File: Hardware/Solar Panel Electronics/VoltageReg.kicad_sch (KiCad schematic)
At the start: 4 parts

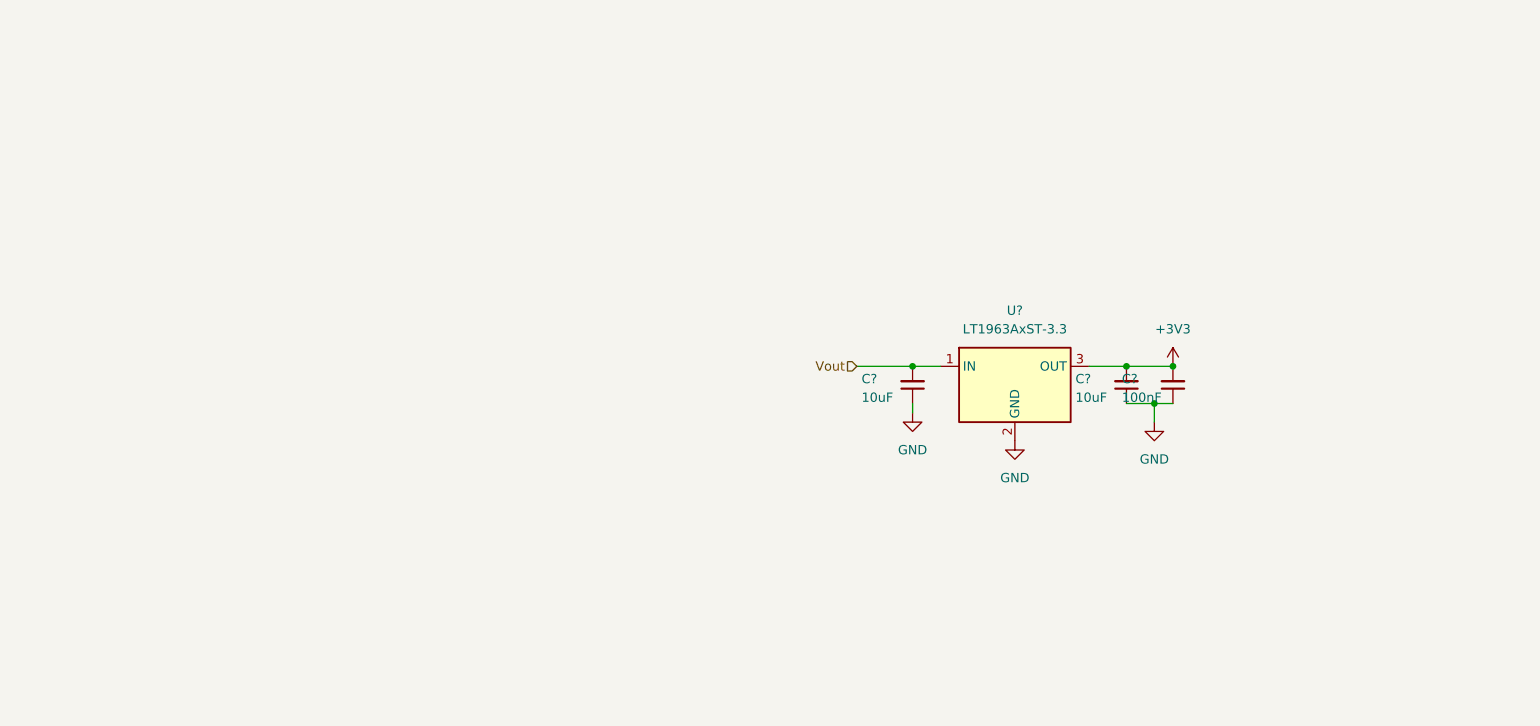
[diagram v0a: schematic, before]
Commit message: Added voltage regulators. Need to size components
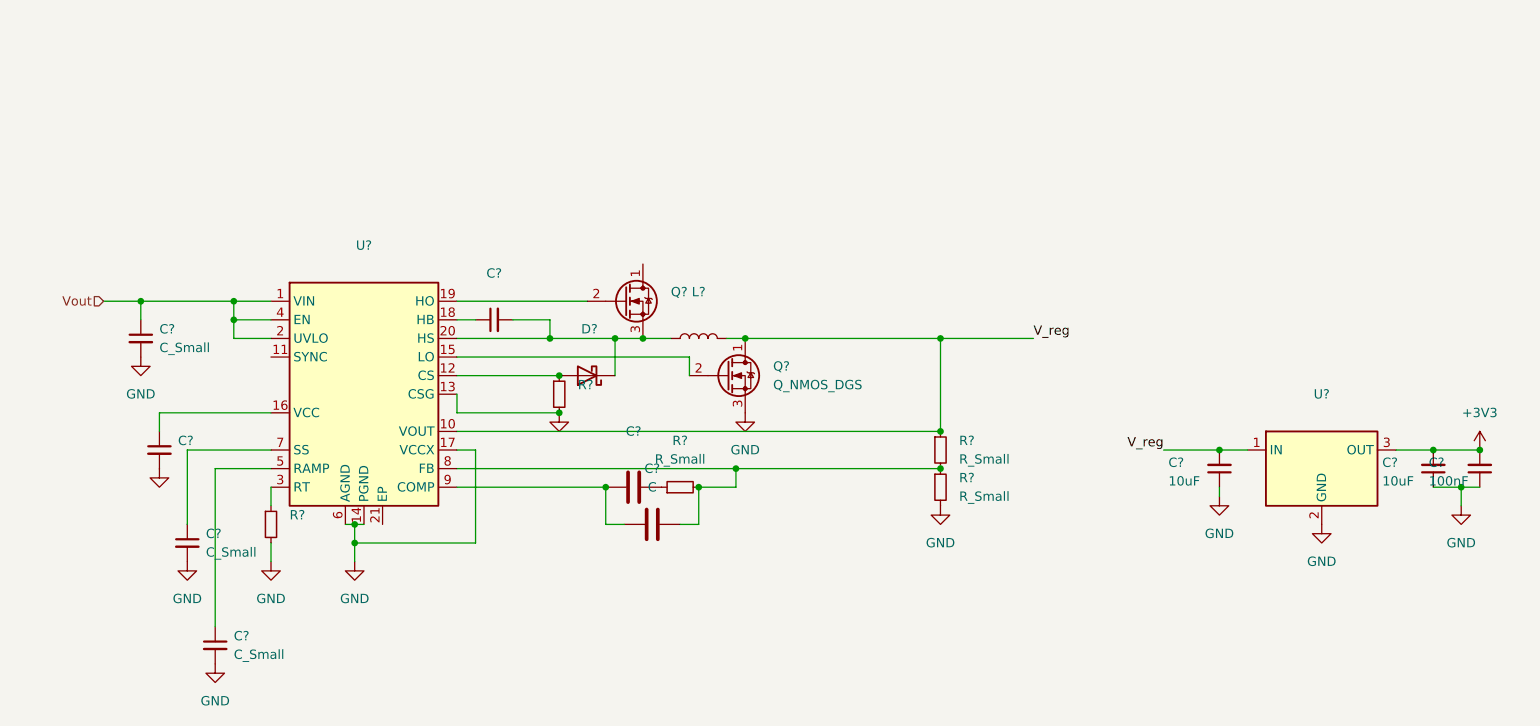
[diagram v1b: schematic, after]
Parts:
- added C? (x2): (no value), symbol Device:C_Small
- added C? (x3): C_Small, symbol Device:C_Small
- added C?: (no value), symbol Device:C
- added C?: C, symbol Device:C
- added D?: (no value), symbol Device:D_Schottky
- added L?: (no value), symbol Device:L
- added Q?: Q_NMOS_DGS, symbol Device:Q_NMOS_DGS
- added Q?: (no value), symbol Device:Q_NMOS_DGS
- added R? (x3): R_Small, symbol Device:R_Small
- added R? (x2): (no value), symbol Device:R_Small
- added U?: (no value), symbol Regulator_Switching:LM5118MH
- U?: value LT1963AxST-3.3 -> (none)
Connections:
- net GND: now also C?.2, C?.2, C?.2, C?.2, Q?.3 (S), R?.2, R?.2, R?.2, U?.13 (CSG), U?.14 (PGND), U?.17 (VCCX), U?.6 (AGND)
- net Vout: now also C?.1, U?.1 (VIN), U?.2 (UVLO), U?.4 (EN); no longer C?.2, U?.1 (IN)
- new net: C?.1, U?.16 (VCC)
- new net: C?.2, D?.1 (K), L?.1, Q?.3 (S), U?.20 (HS)
- new net: D?.2 (A), R?.1, U?.12 (CS)
- new net: Q?.2 (G), U?.15 (LO)
- new net: C?.1, U?.18 (HB)
- new net: Q?.2 (G), U?.19 (HO)
- new net: R?.1, U?.3 (RT)
- new net: C?.1, U?.5 (RAMP)
- new net: C?.1, U?.7 (SS)
- new net: C?.1, R?.1, R?.2, R?.2, U?.8 (FB)
- new net: C?.2, C?.2, U?.9 (COMP)
- new net: C?.1, R?.1
- new net V_reg: C?.2, L?.2, Q?.1 (D), R?.1, U?.1 (IN), U?.10 (VOUT)
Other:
- moved on the sheet: C?, U?

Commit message: Changed to use ADS131M04 adc instead of esp32 adc for power calculation
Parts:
- C? (x2): value (none) -> C_Small
- C?: value (none) -> C
- D?: value (none) -> D_Schottky
- L?: value (none) -> L
- Q?: value (none) -> Q_NMOS_DGS
- R? (x2): value (none) -> R_Small
- U?: value (none) -> LM5118MH; footprint (none) -> Package_SO:Texas_PWP0020A
- U?: value (none) -> LT1963AxST-3.3
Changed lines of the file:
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@@
       (effects (font (size 1.27 1.27)) (justify left))
     )
-    (property "Value" "" (id 1) (at 31.75 92.7162 0)
+    (property "Value" "C_Small" (id 1) (at 31.75 92.7162 0)
       (effects (font (size 1.27 1.27)) (justify left))
     )
@@
     (in_bom yes) (on_board yes) (fields_autoplaced)
     (property "Reference" "D?" (id 0) (at 87.9475 74.93 0))
-    (property "Value" "" (id 1) (at 87.9475 77.47 0))
+    (property "Value" "D_Schottky" (id 1) (at 87.9475 77.47 0))
     (property "Footprint" "" (id 2) (at 87.63 81.28 0)
       (effects (font (size 1.27 1.27)) hide)
@@
     (in_bom yes) (on_board yes) (fields_autoplaced)
     (property "Reference" "C?" (id 0) (at 74.9363 67.31 90))
-    (property "Value" "" (id 1) (at 74.9363 69.85 90))
+    (property "Value" "C_Small" (id 1) (at 74.9363 69.85 90))
     (property "Footprint" "" (id 2) (at 74.93 73.66 0)
       (effects (font (size 1.27 1.27)) hide)
@@
     (in_bom yes) (on_board yes) (fields_autoplaced)
     (property "Reference" "U?" (id 0) (at 57.15 63.5 0))
-    (property "Value" "" (id 1) (at 57.15 66.04 0))
-    (property "Footprint" "" (id 2) (at 74.93 67.31 0)
+    (property "Value" "LM5118MH" (id 1) (at 57.15 66.04 0))
+    (property "Footprint" "Package_SO:Texas_PWP0020A" (id 2) (at 74.93 67.31 0)
       (effects (font (size 1.27 1.27)) (justify left) hide)
     )
@@
       (effects (font (size 1.27 1.27)) (justify left))
     )
-    (property "Value" "" (id 1) (at 86.36 85.0899 0)
+    (property "Value" "R_Small" (id 1) (at 86.36 85.0899 0)
       (effects (font (size 1.27 1.27)) (justify left))
     )
@@
       (effects (font (size 1.27 1.27)) hide)
     )
-    (property "Value" "" (id 1) (at 83.82 91.44 0))
+    (property "Value" "GND" (id 1) (at 83.82 91.44 0))
     (property "Footprint" "" (id 2) (at 83.82 86.36 0)
       (effects (font (size 1.27 1.27)) hide)
@@
       (effects (font (size 1.27 1.27)) (justify left))
     )
-    (property "Value" "" (id 1) (at 99.06 72.3899 0)
+    (property "Value" "Q_NMOS_DGS" (id 1) (at 99.06 72.3899 0)
       (effects (font (size 1.27 1.27)) (justify left))
     )
@@
     (in_bom yes) (on_board yes) (fields_autoplaced)
     (property "Reference" "C?" (id 0) (at 93.98 88.9 90))
-    (property "Value" "" (id 1) (at 93.98 91.44 90))
+    (property "Value" "C" (id 1) (at 93.98 91.44 90))
     (property "Footprint" "" (id 2) (at 90.17 97.4852 0)
       (effects (font (size 1.27 1.27)) hide)
@@
       (effects (font (size 1.27 1.27)) (justify left))
     )
-    (property "Value" "" (id 1) (at 46.99 102.8699 0)
+    (property "Value" "R_Small" (id 1) (at 46.99 102.8699 0)
       (effects (font (size 1.27 1.27)) (justify left))
     )
@@
     (in_bom yes) (on_board yes) (fields_autoplaced)
     (property "Reference" "U?" (id 0) (at 187.96 83.82 0))
-    (property "Value" "" (id 1) (at 187.96 86.36 0))
+    (property "Value" "LT1963AxST-3.3" (id 1) (at 187.96 86.36 0))
     (property "Footprint" "Package_TO_SOT_SMD:SOT-223-3_TabPin2" (id 2) (at 187.96 105.41 0)
       (effects (font (size 1.27 1.27)) hide)
@@
       (effects (font (size 1.27 1.27)) hide)
     )
-    (property "Value" "" (id 1) (at 29.21 99.06 0))
+    (property "Value" "GND" (id 1) (at 29.21 99.06 0))
     (property "Footprint" "" (id 2) (at 29.21 93.98 0)
       (effects (font (size 1.27 1.27)) hide)
@@
     (in_bom yes) (on_board yes) (fields_autoplaced)
     (property "Reference" "L?" (id 0) (at 102.87 69.85 90))
-    (property "Value" "" (id 1) (at 102.87 72.39 90))
+    (property "Value" "L" (id 1) (at 102.87 72.39 90))
     (property "Footprint" "" (id 2) (at 102.87 76.2 0)
       (effects (font (size 1.27 1.27)) hide)

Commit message: Assigned Footprints (preliminary - just to do a quick layout)
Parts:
- gave numbers to parts that had none: 21

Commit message: Add Antenna
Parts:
- C21, C22, C23, C24, C25, C26, C27: footprint (none) -> Capacitor_SMD:C_0603_1608Metric
- D13: footprint (none) -> Diode_SMD:D_SOD-128
- L2: footprint (none) -> Inductor_SMD:L_0603_1608Metric
- Q2, Q3: footprint (none) -> Package_TO_SOT_SMD:SOT-23
- R35, R36, R37, R38, R39: footprint (none) -> Resistor_SMD:R_0603_1608Metric
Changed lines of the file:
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@@
       (effects (font (size 1.27 1.27)) (justify left))
     )
-    (property "Footprint" "" (id 2) (at 29.21 91.44 0)
+    (property "Footprint" "Capacitor_SMD:C_0603_1608Metric" (id 2) (at 29.21 91.44 0)
       (effects (font (size 1.27 1.27)) hide)
     )
@@
       (effects (font (size 1.27 1.27)) (justify left))
     )
-    (property "Footprint" "" (id 2) (at 26.67 76.2 0)
+    (property "Footprint" "Capacitor_SMD:C_0603_1608Metric" (id 2) (at 26.67 76.2 0)
       (effects (font (size 1.27 1.27)) hide)
     )
@@
     (property "Reference" "D13" (id 0) (at 87.9475 74.93 0))
     (property "Value" "D_Schottky" (id 1) (at 87.9475 77.47 0))
-    (property "Footprint" "" (id 2) (at 87.63 81.28 0)
+    (property "Footprint" "Diode_SMD:D_SOD-128" (id 2) (at 87.63 81.28 0)
       (effects (font (size 1.27 1.27)) hide)
     )
@@
       (effects (font (size 1.27 1.27)) (justify left))
     )
-    (property "Footprint" "" (id 2) (at 111.76 78.74 0)
+    (property "Footprint" "Package_TO_SOT_SMD:SOT-23" (id 2) (at 111.76 78.74 0)
       (effects (font (size 1.27 1.27)) hide)
     )
@@
     (property "Reference" "C25" (id 0) (at 74.9363 67.31 90))
     (property "Value" "C_Small" (id 1) (at 74.9363 69.85 90))
-    (property "Footprint" "" (id 2) (at 74.93 73.66 0)
+    (property "Footprint" "Capacitor_SMD:C_0603_1608Metric" (id 2) (at 74.93 73.66 0)
       (effects (font (size 1.27 1.27)) hide)
     )
@@
     (property "Reference" "R37" (id 0) (at 100.33 90.17 90))
     (property "Value" "R_Small" (id 1) (at 100.33 92.71 90))
-    (property "Footprint" "" (id 2) (at 100.33 96.52 0)
+    (property "Footprint" "Resistor_SMD:R_0603_1608Metric" (id 2) (at 100.33 96.52 0)
       (effects (font (size 1.27 1.27)) hide)
     )
@@
       (effects (font (size 1.27 1.27)) (justify left))
     )
-    (property "Footprint" "" (id 2) (at 135.89 96.52 0)
+    (property "Footprint" "Resistor_SMD:R_0603_1608Metric" (id 2) (at 135.89 96.52 0)
       (effects (font (size 1.27 1.27)) hide)
     )
@@
       (effects (font (size 1.27 1.27)) (justify left))
     )
-    (property "Footprint" "" (id 2) (at 83.82 83.82 0)
+    (property "Footprint" "Resistor_SMD:R_0603_1608Metric" (id 2) (at 83.82 83.82 0)
       (effects (font (size 1.27 1.27)) hide)
     )
@@
       (effects (font (size 1.27 1.27)) (justify left))
     )
-    (property "Footprint" "" (id 2) (at 97.79 68.58 0)
+    (property "Footprint" "Package_TO_SOT_SMD:SOT-23" (id 2) (at 97.79 68.58 0)
       (effects (font (size 1.27 1.27)) hide)
     )
@@
     (property "Reference" "C26" (id 0) (at 93.98 88.9 90))
     (property "Value" "C" (id 1) (at 93.98 91.44 90))
-    (property "Footprint" "" (id 2) (at 90.17 97.4852 0)
+    (property "Footprint" "Capacitor_SMD:C_0603_1608Metric" (id 2) (at 90.17 97.4852 0)
       (effects (font (size 1.27 1.27)) hide)
     )
@@
     (property "Reference" "C27" (id 0) (at 96.52 93.98 90))
     (property "Value" "C" (id 1) (at 96.52 96.52 90))
-    (property "Footprint" "" (id 2) (at 92.71 102.5652 0)
+    (property "Footprint" "Capacitor_SMD:C_0603_1608Metric" (id 2) (at 92.71 102.5652 0)
       (effects (font (size 1.27 1.27)) hide)
     )
@@
       (effects (font (size 1.27 1.27)) (justify left))
     )
-    (property "Footprint" "" (id 2) (at 33.02 104.14 0)
+    (property "Footprint" "Capacitor_SMD:C_0603_1608Metric" (id 2) (at 33.02 104.14 0)
       (effects (font (size 1.27 1.27)) hide)
     )
@@
       (effects (font (size 1.27 1.27)) (justify left))
     )
-    (property "Footprint" "" (id 2) (at 135.89 91.44 0)
+    (property "Footprint" "Resistor_SMD:R_0603_1608Metric" (id 2) (at 135.89 91.44 0)
       (effects (font (size 1.27 1.27)) hide)
     )
@@
       (effects (font (size 1.27 1.27)) (justify left))
     )
-    (property "Footprint" "" (id 2) (at 44.45 101.6 0)
+    (property "Footprint" "Resistor_SMD:R_0603_1608Metric" (id 2) (at 44.45 101.6 0)
       (effects (font (size 1.27 1.27)) hide)
     )
@@
       (effects (font (size 1.27 1.27)) (justify left))
     )
-    (property "Footprint" "" (id 2) (at 36.83 118.11 0)
+    (property "Footprint" "Capacitor_SMD:C_0603_1608Metric" (id 2) (at 36.83 118.11 0)
       (effects (font (size 1.27 1.27)) hide)
     )
@@
     (property "Reference" "L2" (id 0) (at 102.87 69.85 90))
     (property "Value" "L" (id 1) (at 102.87 72.39 90))
-    (property "Footprint" "" (id 2) (at 102.87 76.2 0)
-      (effects (font (size 1.27 1.27)) hide)
-    )
+    (property "Footprint" "Inductor_SMD:L_0603_1608Metric" (id 2) (at 102.87 76.2 0)
+      (effects (font (size 1.27 1.27)) hide)
+    )

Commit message: Started pcb layout
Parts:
- added J14: (no value), symbol Connector:Screw_Terminal_01x02
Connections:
- net GND: now also J14.2 (Pin_2)
- net V_reg: now also J14.1 (Pin_1)
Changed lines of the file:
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@@
   (junction (at 209.55 91.44) (diameter 0) (color 0 0 0 0)
   )
+  (junction (at 142.24 76.2) (diameter 0) (color 0 0 0 0)
+  )
   (junction (at 107.95 93.98) (diameter 0) (color 0 0 0 0)
   )
@@
     (stroke (width 0) (type default) (color 0 0 0 0))
   )
+  (wire (pts (xy 142.24 76.2) (xy 148.59 76.2))
+    (stroke (width 0) (type default) (color 0 0 0 0))
+  )
   (wire (pts (xy 69.85 96.52) (xy 90.17 96.52))
     (stroke (width 0) (type default) (color 0 0 0 0))
   )
+  (wire (pts (xy 142.24 76.2) (xy 142.24 34.29))
+    (stroke (width 0) (type default) (color 0 0 0 0))
+  )
   (wire (pts (xy 69.85 86.36) (xy 83.82 86.36))
     (stroke (width 0) (type default) (color 0 0 0 0))
   )
+  (wire (pts (xy 175.26 36.83) (xy 175.26 43.18))
+    (stroke (width 0) (type default) (color 0 0 0 0))
+  )
   (wire (pts (xy 135.89 88.9) (xy 135.89 76.2))
     (stroke (width 0) (type default) (color 0 0 0 0))
@@
     (stroke (width 0) (type default) (color 0 0 0 0))
   )
+  (wire (pts (xy 181.61 36.83) (xy 175.26 36.83))
+    (stroke (width 0) (type default) (color 0 0 0 0))
+  )
   (wire (pts (xy 29.21 86.36) (xy 29.21 88.9))
     (stroke (width 0) (type default) (color 0 0 0 0))
@@
     (stroke (width 0) (type default) (color 0 0 0 0))
   )
+  (wire (pts (xy 142.24 34.29) (xy 181.61 34.29))
+    (stroke (width 0) (type default) (color 0 0 0 0))
+  )
   (wire (pts (xy 95.25 76.2) (xy 99.06 76.2))
     (stroke (width 0) (type default) (color 0 0 0 0))
@@
     (stroke (width 0) (type default) (color 0 0 0 0))
   )
-  (wire (pts (xy 135.89 76.2) (xy 148.59 76.2))
+  (wire (pts (xy 135.89 76.2) (xy 142.24 76.2))
     (stroke (width 0) (type default) (color 0 0 0 0))
   )
@@
     )
     (property "Datasheet" "~" (id 3) (at 29.21 91.44 0)
+      (effects (font (size 1.27 1.27)) hide)
+    )
+    (pin "1")
+    (pin "2")
+  )
+  (symbol (lib_id "Connector:Screw_Terminal_01x02") (at 186.69 34.29 0) (unit 1)
+    (in_bom yes) (on_board yes) (fields_autoplaced)
+    (property "Reference" "J14" (id 0) (at 189.23 34.2899 0)
+      (effects (font (size 1.27 1.27)) (justify left))
+    )
+    (property "Value" "" (id 1) (at 189.23 36.8299 0)
+      (effects (font (size 1.27 1.27)) (justify left))
+    )
+    (property "Footprint" "" (id 2) (at 186.69 34.29 0)
+      (effects (font (size 1.27 1.27)) hide)
+    )
+    (property "Datasheet" "~" (id 3) (at 186.69 34.29 0)
       (effects (font (size 1.27 1.27)) hide)
     )
@@
     (pin "2")
   )
+  (symbol (lib_id "power:GND") (at 175.26 43.18 0) (unit 1)
+    (in_bom yes) (on_board yes) (fields_autoplaced)
+    (property "Reference" "#PWR0138" (id 0) (at 175.26 49.53 0)
+      (effects (font (size 1.27 1.27)) hide)
+    )
+    (property "Value" "" (id 1) (at 175.26 48.26 0))
+    (property "Footprint" "" (id 2) (at 175.26 43.18 0)
+      (effects (font (size 1.27 1.27)) hide)
+    )
+    (property "Datasheet" "" (id 3) (at 175.26 43.18 0)
+      (effects (font (size 1.27 1.27)) hide)
+    )
+    (pin "1")
+  )
   (symbol (lib_id "power:+3V3") (at 209.55 91.44 0) (unit 1)

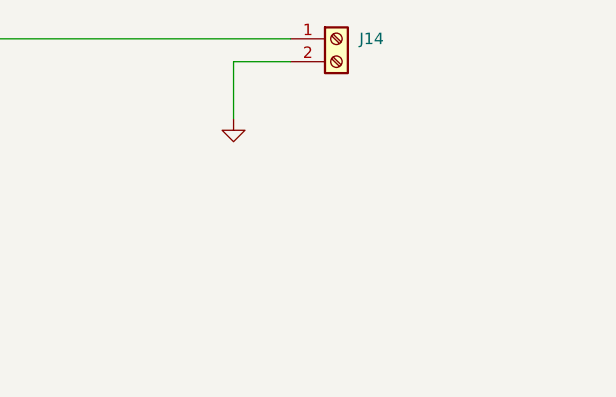
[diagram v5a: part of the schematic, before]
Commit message: Preliminary Layout done. (46x77mm)
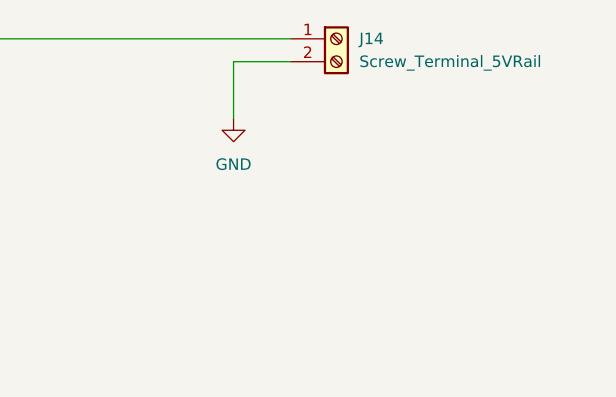
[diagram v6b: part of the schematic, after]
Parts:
- J14: value (none) -> Screw_Terminal_5VRail; footprint (none) -> TerminalBlock_TE-Connectivity:TerminalBlock_TE_282834-2_1x02_P2.54mm_Horizontal
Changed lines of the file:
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@@
       (effects (font (size 1.27 1.27)) (justify left))
     )
-    (property "Value" "" (id 1) (at 189.23 36.8299 0)
-      (effects (font (size 1.27 1.27)) (justify left))
-    )
-    (property "Footprint" "" (id 2) (at 186.69 34.29 0)
+    (property "Value" "Screw_Terminal_5VRail" (id 1) (at 189.23 36.8299 0)
+      (effects (font (size 1.27 1.27)) (justify left))
+    )
+    (property "Footprint" "TerminalBlock_TE-Connectivity:TerminalBlock_TE_282834-2_1x02_P2.54mm_Horizontal" (id 2) (at 186.69 34.29 0)
       (effects (font (size 1.27 1.27)) hide)
     )
@@
       (effects (font (size 1.27 1.27)) hide)
     )
-    (property "Value" "" (id 1) (at 175.26 48.26 0))
+    (property "Value" "GND" (id 1) (at 175.26 48.26 0))
     (property "Footprint" "" (id 2) (at 175.26 43.18 0)
       (effects (font (size 1.27 1.27)) hide)
